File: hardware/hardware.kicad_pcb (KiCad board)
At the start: 2 copper layers, 76 x 60.5 mm, 159 parts, among them J1 USB_B_Micro, U1 CH32V003F4P6, U10 CH32V003F4P6, U11 CH32V003F4P6, U12 CH32V003F4P6, U13 CH32V003F4P6, U14 CH32V003F4P6, U15 CH32V003F4P6, U16 CH32V003F4P6, U17 CH32V003F4P6, U18 CH32V003F4P6, U19 CH32V003F4P6, U2 CH32V003F4P6, U20 CH32V003F4P6, U21 CH32V003F4P6, U22 CH32V003F4P6, U23 CH32V003F4P6, U24 CH32V003F4P6, U25 CH32V003F4P6, U26 CH32V003F4P6, U27 CH32V003F4P6, U3 AMS1117-3.3, U4 CH340C, U5 CH32V003F4P6, U6 CH32V003F4P6, U7 CH32V003F4P6, U8 CH32V003F4P6, U9 CH32V003F4P6

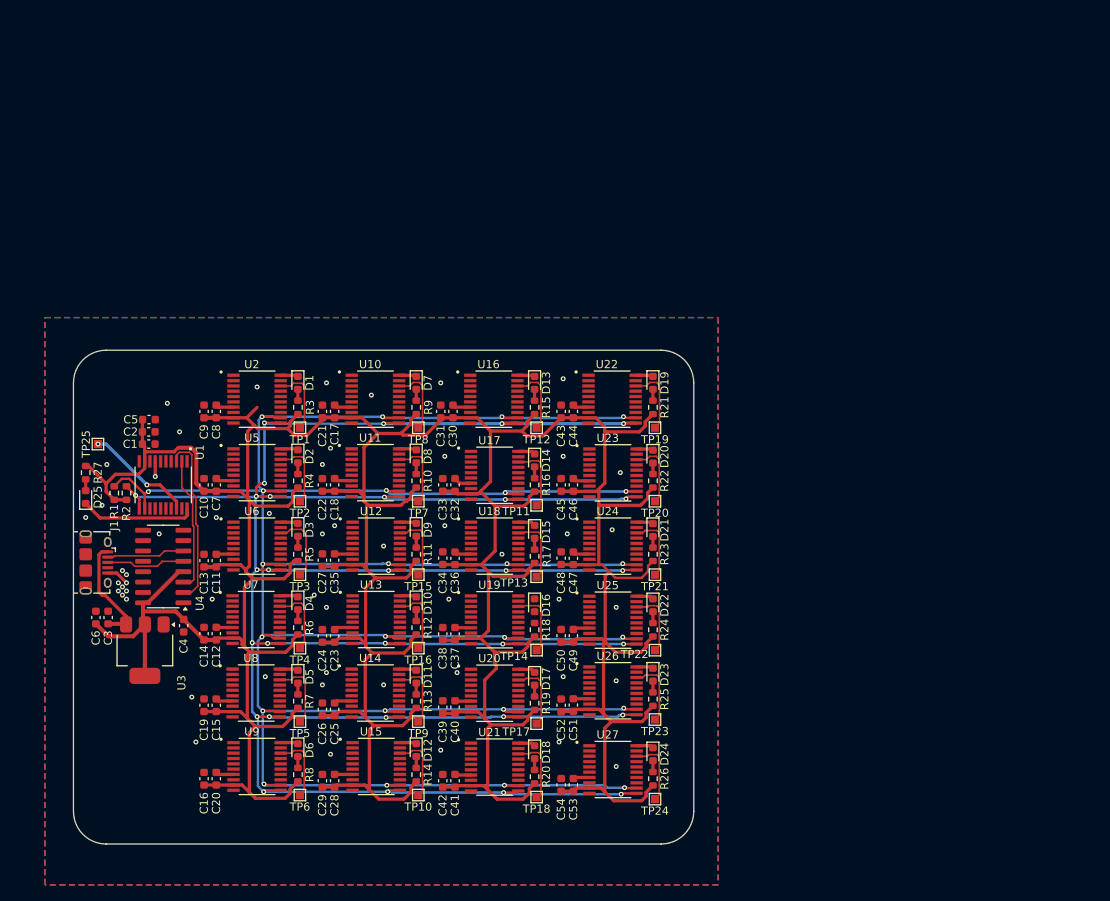
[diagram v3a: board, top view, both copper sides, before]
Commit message: add ethernet wiring
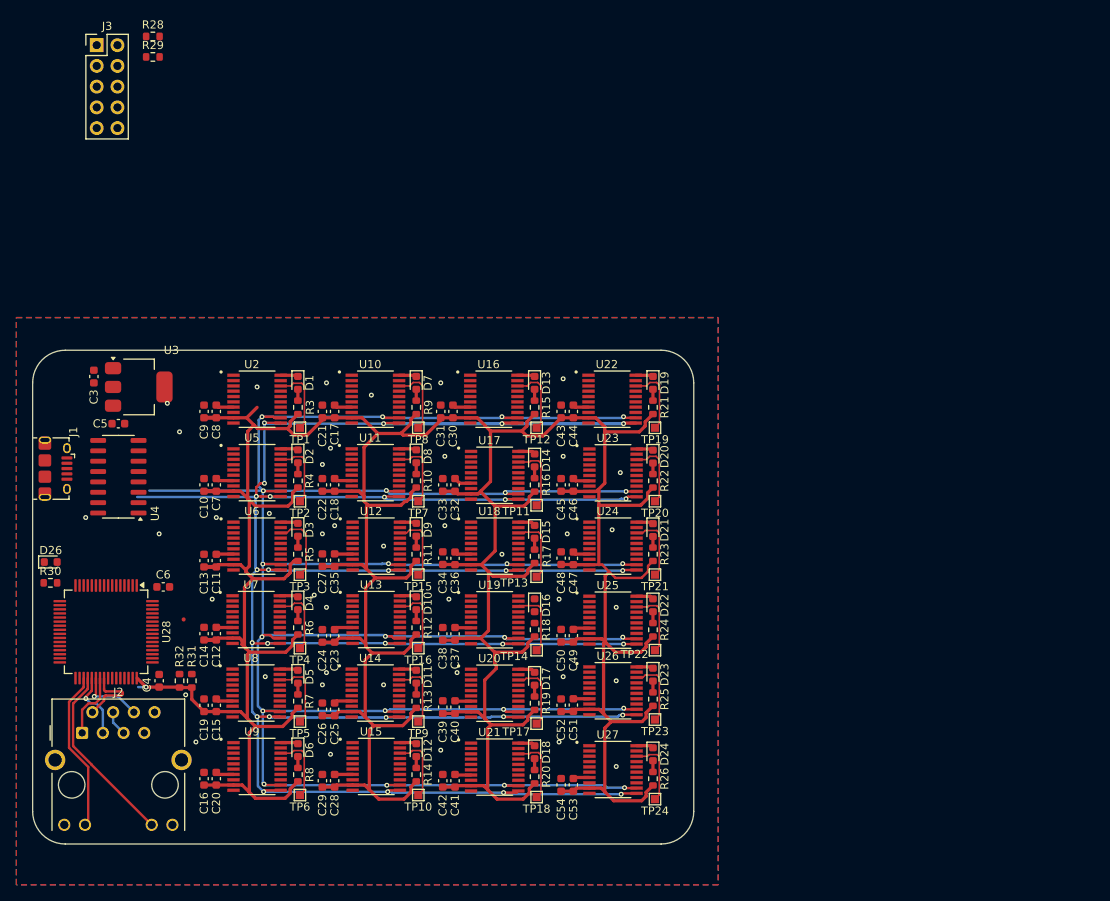
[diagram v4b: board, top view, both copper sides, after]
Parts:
- removed C1, C2: C_Small, Capacitor_SMD:C_0603_1608Metric
- removed D25: LED, LED_SMD:LED_0603_1608Metric
- removed R1, R2, R27: R_Small, Resistor_SMD:R_0603_1608Metric
- removed TP25: TestPoint, TestPoint:TestPoint_Pad_1.0x1.0mm
- removed U1: CH32V003F4P6, CH32V003F4P6:SOP65P640X121-20N
- added D26: LED, LED_SMD:LED_0603_1608Metric, F.Cu at (37.7, 69.0)
- added J2: RJ45_Hanrun_HR911105A_Horizontal, Connector_RJ:RJ45_Hanrun_HR911105A_Horizontal, F.Cu at (41.6, 89.9)
- added J3: Conn_02x05_Odd_Even, Connector_PinHeader_2.54mm:PinHeader_2x05_P2.54mm_Vertical, F.Cu at (43.4, 5.62)
- added R28: R_Small, Resistor_SMD:R_0603_1608Metric, F.Cu at (50.2, 4.55)
- added R29: R_Small, Resistor_SMD:R_0603_1608Metric, F.Cu at (50.2, 7.07)
- added R30: R_Small, Resistor_SMD:R_0603_1608Metric, F.Cu at (37.7, 71.5)
- added R31: R_Small, Resistor_SMD:R_0603_1608Metric, F.Cu at (55.0, 83.5)
- added R32: R_Small, Resistor_SMD:R_0603_1608Metric, F.Cu at (53.5, 83.5)
- added U28: CH32V307RCT6, Package_QFP:LQFP-64_10x10mm_P0.5mm, F.Cu at (44.5, 77.5)
- moved U3 32.3 mm to (48.5, 47.5), turned to 0 degrees
- moved C3 29.6 mm to (43.0, 46.2)
- moved J1 12.5 mm to (38.3, 57.5)
- moved U4 12.3 mm to (46.0, 58.5)
- moved C6 9.06 mm to (51.5, 72.0), turned to 0 degrees
- moved C4 7.39 mm to (51.0, 83.5), turned to 90 degrees
- moved C5 3.78 mm to (46.0, 52.0)
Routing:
- net +3V3: track 572.7 -> 524.9 mm, vias 0 -> 1
- net LED1: track 0.00 -> 22.7 mm
- net TX-PROG: track 21.4 -> 0.00 mm
- net LED2: track 0.00 -> 19.9 mm
- net RX-PROG: track 16.5 -> 0.00 mm
- net Net-(D25-K): track 14.1 -> 0.00 mm
- net +5V: track 13.6 -> 0.00 mm
- net Net-(U1-PD1/SWIO/T1CH3N/AETR2): track 13.4 -> 0.00 mm, vias 2 -> 0
- net D+: track 9.73 -> 0.00 mm
- net D-: track 9.59 -> 0.00 mm
- net TDN: track 0.00 -> 8.99 mm
- net RDP: track 0.00 -> 8.28 mm, vias 0 -> 1
- net TDP: track 0.00 -> 8.12 mm
- net RDN: track 0.00 -> 7.98 mm, vias 0 -> 1
- net SCL: track 378.0 -> 370.6 mm, vias 25 -> 24
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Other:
- board size 76 x 60.5 mm -> 81 x 60.5 mm

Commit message: wiring ch32v307 + ethernet
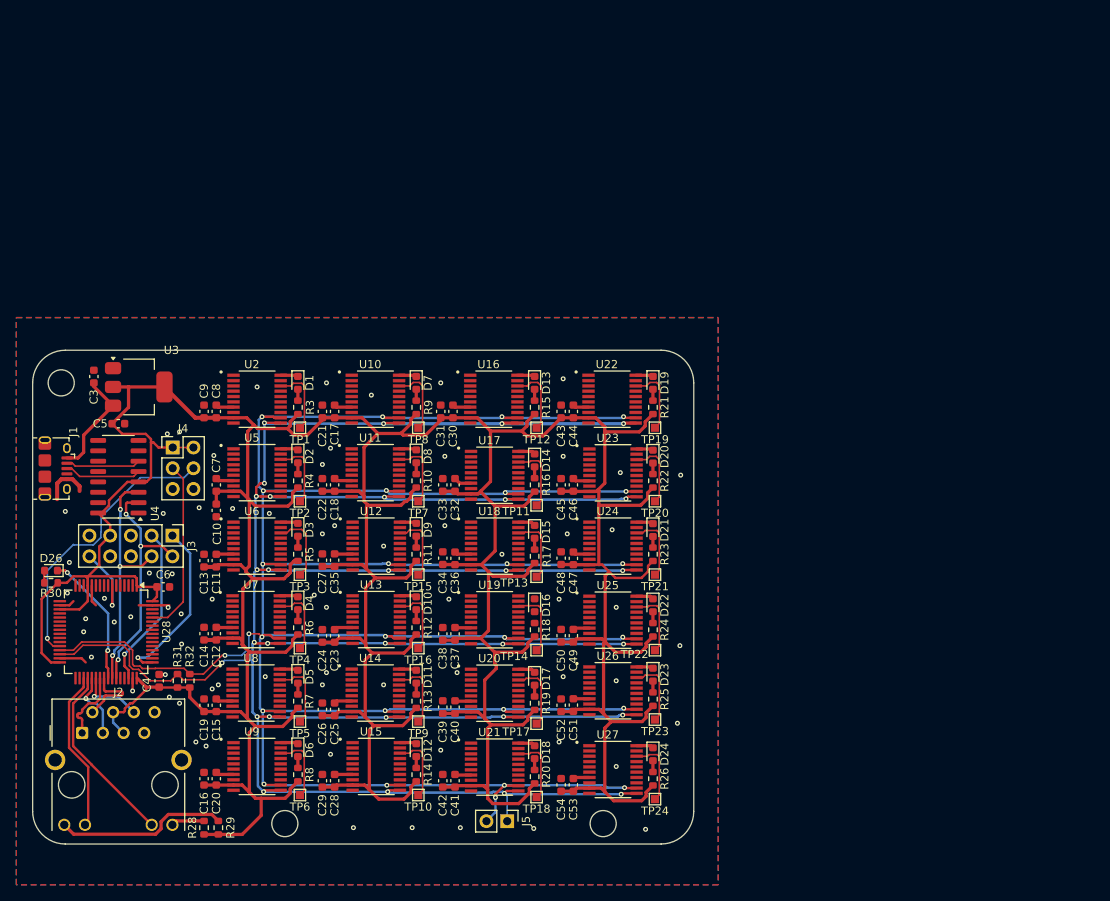
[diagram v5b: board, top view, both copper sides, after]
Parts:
- added J4: Conn_02x03_Odd_Even, Connector_PinHeader_2.54mm:PinHeader_2x03_P2.54mm_Vertical, F.Cu at (52.7, 54.9)
- added J5: Conn_01x02, Connector_PinHeader_2.54mm:PinHeader_1x02_P2.54mm_Vertical, F.Cu at (93.6, 100.7)
- moved R28 97.1 mm to (56.5, 101.5), turned to 90 degrees
- moved R29 94.8 mm to (58.2, 101.5), turned to 90 degrees
- moved J3 60.8 mm to (52.6, 65.7), turned to -90 degrees
- moved C10 3.47 mm to (58.0, 62.6), turned to -90 degrees
- moved R31 1.75 mm to (53.2, 83.5)
- moved R32 1.25 mm to (54.8, 83.5)
- moved D26 1.05 mm to (37.8, 70.0), turned to 180 degrees
- moved R30 0.08 mm to (37.8, 71.5)
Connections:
- J3 pad 2: TX -> TX-PROG
- J3 pad 4: RX -> RX-PROG
- U28 pad 52: LED2 -> unconnected-(U28-PC11-Pad52)
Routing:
- net +3V3: track 524.9 -> 625.5 mm, vias 1 -> 0
- net BOOT1: track 0.00 -> 35.0 mm, vias 0 -> 1
- net RX-PROG: track 0.00 -> 29.5 mm, vias 0 -> 3
- net TX-PROG: track 0.00 -> 29.3 mm, vias 0 -> 3
- net SCL: track 370.6 -> 392.9 mm, vias 24 -> 27
- net BOOT0: track 0.00 -> 21.5 mm
- net SWCLK: track 0.00 -> 21.2 mm, vias 0 -> 1
- net Net-(J2-Pad9): track 0.00 -> 21.2 mm
- net SWDIO: track 0.00 -> 20.0 mm, vias 0 -> 1
- net GND: track 50.7 -> 69.8 mm, vias 42 -> 72
- net SDA: track 370.9 -> 388.4 mm, vias 29 -> 30
- net Net-(D26-K): track 0.00 -> 16.5 mm, vias 0 -> 2
- net +5V: track 0.00 -> 13.3 mm
- net RST: track 0.00 -> 9.58 mm, vias 0 -> 1
- net D+: track 0.00 -> 9.42 mm
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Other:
- outline, holes or cut-outs redrawn

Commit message: add external crystal
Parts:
- added C1: 10pf, Capacitor_SMD:C_0603_1608Metric, F.Cu at (43.0, 68.5)
- added C2: 10pf, Capacitor_SMD:C_0603_1608Metric, F.Cu at (48.8, 68.5)
- added Y1: Crystal, Crystal:Crystal_SMD_3225-4Pin_3.2x2.5mm, F.Cu at (45.9, 68.6)
- moved J4 18.6 mm to (40.4, 68.9), turned to 180 degrees
- moved D26 12.8 mm to (37.6, 82.8)
- moved R30 12.8 mm to (37.6, 84.3)
- moved J3 2.59 mm to (55.1, 65.1), turned to 180 degrees
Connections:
- U28 pad 5: unconnected-(U28-OSC_IN/PD0-Pad5) -> XTAL2
- U28 pad 6: unconnected-(U28-OSC_OUT/PD1-Pad6) -> XTAL1
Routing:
- net BOOT1: track 35.0 -> 14.7 mm
- net RST: track 9.58 -> 26.5 mm
- net Net-(D26-K): track 16.5 -> 7.70 mm, vias 2 -> 0
- net XTAL1: track 0.00 -> 7.68 mm
- net XTAL2: track 0.00 -> 7.48 mm
- net BOOT0: track 21.5 -> 16.7 mm, vias 0 -> 1
- net SWDIO: track 20.0 -> 24.3 mm
- net +3V3: track 625.5 -> 628.6 mm
- net TX-PROG: track 29.3 -> 26.9 mm, vias 3 -> 1
- net Net-(D16-K): track 0.00 -> 2.15 mm
- net Net-(D16-A): track 0.00 -> 1.39 mm
- net RX-PROG: track 29.5 -> 28.7 mm, vias 3 -> 1
- net GND: vias 72 -> 69

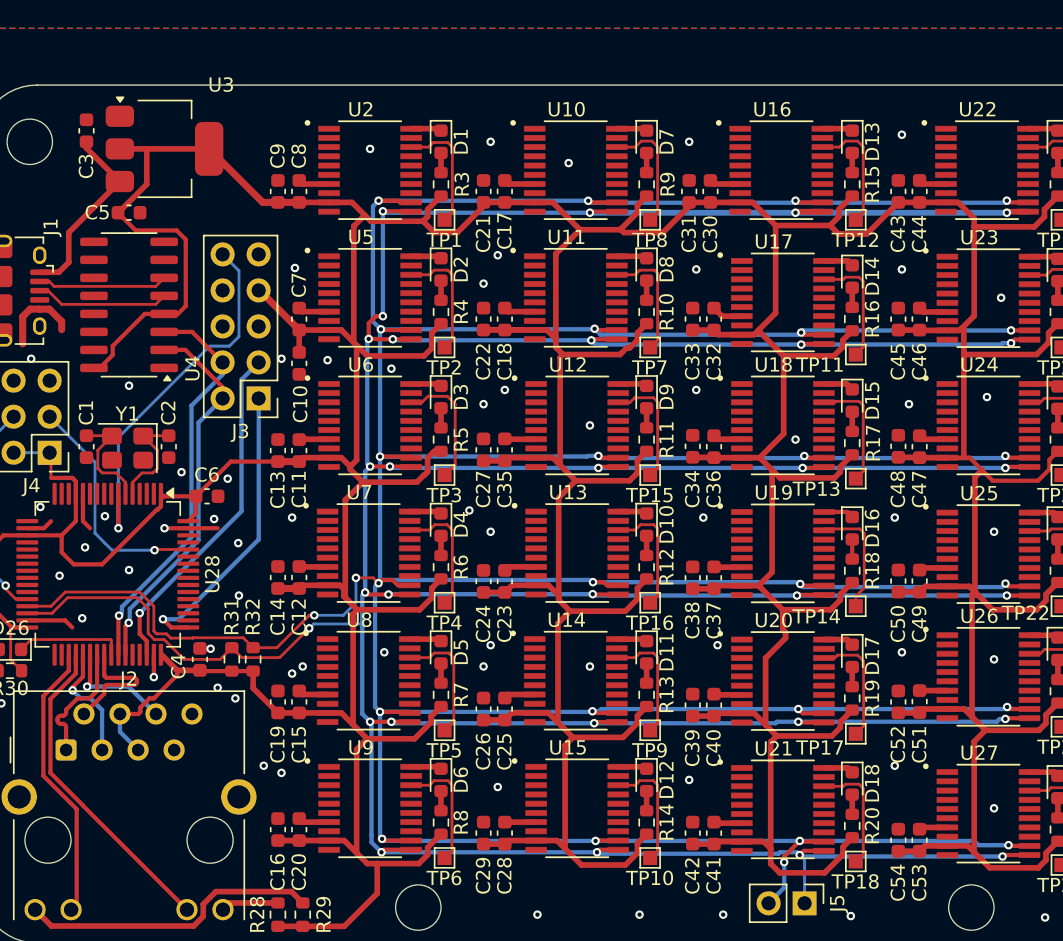
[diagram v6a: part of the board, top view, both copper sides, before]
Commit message: update crystal + slave reset pull up
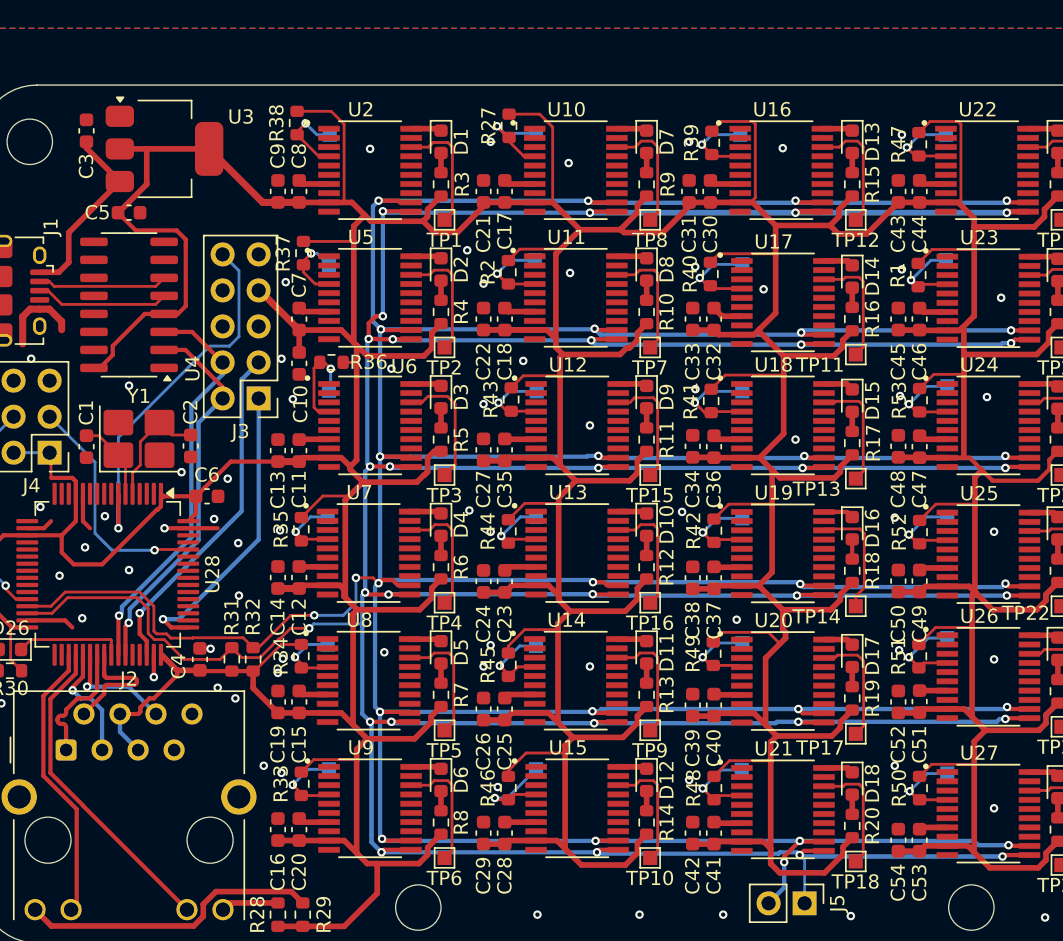
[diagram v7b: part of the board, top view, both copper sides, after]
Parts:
- added R1: R_Small, Resistor_SMD:R_0603_1608Metric, F.Cu at (101.7, 56.4)
- added R2: R_Small, Resistor_SMD:R_0603_1608Metric, F.Cu at (72.8, 56.2)
- added R27: R_Small, Resistor_SMD:R_0603_1608Metric, F.Cu at (72.8, 45.9)
- added R33: R_Small, Resistor_SMD:R_0603_1608Metric, F.Cu at (58.1, 92.3)
- added R34: R_Small, Resistor_SMD:R_0603_1608Metric, F.Cu at (58.1, 83.3)
- added R35: R_Small, Resistor_SMD:R_0603_1608Metric, F.Cu at (58.1, 74.3)
- added R36: R_Small, Resistor_SMD:R_0603_1608Metric, F.Cu at (60.3, 62.5)
- added R37: R_Small, Resistor_SMD:R_0603_1608Metric, F.Cu at (58.3, 54.9)
- added R38: R_Small, Resistor_SMD:R_0603_1608Metric, F.Cu at (57.9, 45.7)
- added R39: R_Small, Resistor_SMD:R_0603_1608Metric, F.Cu at (87.1, 47.1)
- added R40: R_Small, Resistor_SMD:R_0603_1608Metric, F.Cu at (87.0, 56.3)
- added R41: R_Small, Resistor_SMD:R_0603_1608Metric, F.Cu at (87.0, 65.3)
- added R42: R_Small, Resistor_SMD:R_0603_1608Metric, F.Cu at (87.2, 74.4)
- added R43: R_Small, Resistor_SMD:R_0603_1608Metric, F.Cu at (73.0, 65.2)
- added R44: R_Small, Resistor_SMD:R_0603_1608Metric, F.Cu at (72.8, 74.5)
- added R45: R_Small, Resistor_SMD:R_0603_1608Metric, F.Cu at (72.8, 83.9)
- added R46: R_Small, Resistor_SMD:R_0603_1608Metric, F.Cu at (72.8, 92.6)
- added R47: R_Small, Resistor_SMD:R_0603_1608Metric, F.Cu at (101.7, 47.2)
- added R48: R_Small, Resistor_SMD:R_0603_1608Metric, F.Cu at (87.2, 92.6)
- added R49: R_Small, Resistor_SMD:R_0603_1608Metric, F.Cu at (87.2, 83.1)
- added R50: R_Small, Resistor_SMD:R_0603_1608Metric, F.Cu at (101.8, 92.6)
- added R51: R_Small, Resistor_SMD:R_0603_1608Metric, F.Cu at (101.7, 83.3)
- added R52: R_Small, Resistor_SMD:R_0603_1608Metric, F.Cu at (101.8, 74.5)
- added R53: R_Small, Resistor_SMD:R_0603_1608Metric, F.Cu at (101.8, 65.2)
- added TP25: TestPoint, TestPoint:TestPoint_Pad_1.0x1.0mm, B.Cu at (103.6, 55.4)
- added TP26: TestPoint, TestPoint:TestPoint_Pad_1.0x1.0mm, B.Cu at (74.6, 55.4)
- added TP27: TestPoint, TestPoint:TestPoint_Pad_1.0x1.0mm, B.Cu at (74.7, 46.4)
- added TP28: TestPoint, TestPoint:TestPoint_Pad_1.0x1.0mm, B.Cu at (60.1, 91.2)
- added TP29: TestPoint, TestPoint:TestPoint_Pad_1.0x1.0mm, B.Cu at (60.0, 82.5)
- added TP30: TestPoint, TestPoint:TestPoint_Pad_1.0x1.0mm, B.Cu at (60.0, 73.5)
- added TP31: TestPoint, TestPoint:TestPoint_Pad_1.0x1.0mm, B.Cu at (60.1, 64.5)
- added TP32: TestPoint, TestPoint:TestPoint_Pad_1.0x1.0mm, B.Cu at (60.1, 55.7)
- added TP33: TestPoint, TestPoint:TestPoint_Pad_1.0x1.0mm, B.Cu at (60.1, 46.5)
- added TP34: TestPoint, TestPoint:TestPoint_Pad_1.0x1.0mm, B.Cu at (89.1, 46.5)
- added TP35: TestPoint, TestPoint:TestPoint_Pad_1.0x1.0mm, B.Cu at (89.2, 55.6)
- added TP36: TestPoint, TestPoint:TestPoint_Pad_1.0x1.0mm, B.Cu at (89.2, 64.6)
- added TP37: TestPoint, TestPoint:TestPoint_Pad_1.0x1.0mm, B.Cu at (89.2, 73.5)
- added TP38: TestPoint, TestPoint:TestPoint_Pad_1.0x1.0mm, B.Cu at (74.8, 64.6)
- added TP39: TestPoint, TestPoint:TestPoint_Pad_1.0x1.0mm, B.Cu at (74.7, 73.5)
- added TP40: TestPoint, TestPoint:TestPoint_Pad_1.0x1.0mm, B.Cu at (74.7, 82.5)
- added TP41: TestPoint, TestPoint:TestPoint_Pad_1.0x1.0mm, B.Cu at (74.7, 91.2)
- added TP42: TestPoint, TestPoint:TestPoint_Pad_1.0x1.0mm, B.Cu at (103.6, 46.5)
- added TP43: TestPoint, TestPoint:TestPoint_Pad_1.0x1.0mm, B.Cu at (89.2, 91.3)
- added TP44: TestPoint, TestPoint:TestPoint_Pad_1.0x1.0mm, B.Cu at (89.2, 82.3)
- added TP45: TestPoint, TestPoint:TestPoint_Pad_1.0x1.0mm, B.Cu at (103.7, 91.5)
- added TP46: TestPoint, TestPoint:TestPoint_Pad_1.0x1.0mm, B.Cu at (103.7, 82.0)
- added TP47: TestPoint, TestPoint:TestPoint_Pad_1.0x1.0mm, B.Cu at (103.7, 73.5)
- added TP48: TestPoint, TestPoint:TestPoint_Pad_1.0x1.0mm, B.Cu at (103.7, 64.2)
- Y1: value Crystal -> Crystal_GND24; footprint Crystal:Crystal_SMD_3225-4Pin_3.2x2.5mm -> Crystal:Crystal_SMD_3225-4Pin_3.2x2.5mm_HandSoldering
- moved C2 1.55 mm to (50.4, 68.5)
- moved Y1 1.03 mm to (46.7, 68.0), turned to 0 degrees
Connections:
- U10 pad 4: unconnected-(U10-PD7/~{RST}/T2CH4/OPP1-Pad4) -> Net-(U10-PD7/~{RST}/T2CH4/OPP1)
- U11 pad 4: unconnected-(U11-PD7/~{RST}/T2CH4/OPP1-Pad4) -> Net-(U11-PD7/~{RST}/T2CH4/OPP1)
- U12 pad 4: unconnected-(U12-PD7/~{RST}/T2CH4/OPP1-Pad4) -> Net-(U12-PD7/~{RST}/T2CH4/OPP1)
- U13 pad 4: unconnected-(U13-PD7/~{RST}/T2CH4/OPP1-Pad4) -> Net-(U13-PD7/~{RST}/T2CH4/OPP1)
- U14 pad 4: unconnected-(U14-PD7/~{RST}/T2CH4/OPP1-Pad4) -> Net-(U14-PD7/~{RST}/T2CH4/OPP1)
- U15 pad 4: unconnected-(U15-PD7/~{RST}/T2CH4/OPP1-Pad4) -> Net-(U15-PD7/~{RST}/T2CH4/OPP1)
- U16 pad 4: unconnected-(U16-PD7/~{RST}/T2CH4/OPP1-Pad4) -> Net-(U16-PD7/~{RST}/T2CH4/OPP1)
- U17 pad 4: unconnected-(U17-PD7/~{RST}/T2CH4/OPP1-Pad4) -> Net-(U17-PD7/~{RST}/T2CH4/OPP1)
- U18 pad 4: unconnected-(U18-PD7/~{RST}/T2CH4/OPP1-Pad4) -> Net-(U18-PD7/~{RST}/T2CH4/OPP1)
- U19 pad 4: unconnected-(U19-PD7/~{RST}/T2CH4/OPP1-Pad4) -> Net-(U19-PD7/~{RST}/T2CH4/OPP1)
- U2 pad 4: unconnected-(U2-PD7/~{RST}/T2CH4/OPP1-Pad4) -> Net-(U2-PD7/~{RST}/T2CH4/OPP1)
- U20 pad 4: unconnected-(U20-PD7/~{RST}/T2CH4/OPP1-Pad4) -> Net-(U20-PD7/~{RST}/T2CH4/OPP1)
- U21 pad 4: unconnected-(U21-PD7/~{RST}/T2CH4/OPP1-Pad4) -> Net-(U21-PD7/~{RST}/T2CH4/OPP1)
- U22 pad 4: unconnected-(U22-PD7/~{RST}/T2CH4/OPP1-Pad4) -> Net-(U22-PD7/~{RST}/T2CH4/OPP1)
- U23 pad 4: unconnected-(U23-PD7/~{RST}/T2CH4/OPP1-Pad4) -> Net-(U23-PD7/~{RST}/T2CH4/OPP1)
- U24 pad 4: unconnected-(U24-PD7/~{RST}/T2CH4/OPP1-Pad4) -> Net-(U24-PD7/~{RST}/T2CH4/OPP1)
- U25 pad 4: unconnected-(U25-PD7/~{RST}/T2CH4/OPP1-Pad4) -> Net-(U25-PD7/~{RST}/T2CH4/OPP1)
- U26 pad 4: unconnected-(U26-PD7/~{RST}/T2CH4/OPP1-Pad4) -> Net-(U26-PD7/~{RST}/T2CH4/OPP1)
- U27 pad 4: unconnected-(U27-PD7/~{RST}/T2CH4/OPP1-Pad4) -> Net-(U27-PD7/~{RST}/T2CH4/OPP1)
- U5 pad 4: unconnected-(U5-PD7/~{RST}/T2CH4/OPP1-Pad4) -> Net-(U5-PD7/~{RST}/T2CH4/OPP1)
- U6 pad 4: unconnected-(U6-PD7/~{RST}/T2CH4/OPP1-Pad4) -> Net-(U6-PD7/~{RST}/T2CH4/OPP1)
- U7 pad 4: unconnected-(U7-PD7/~{RST}/T2CH4/OPP1-Pad4) -> Net-(U7-PD7/~{RST}/T2CH4/OPP1)
- U8 pad 4: unconnected-(U8-PD7/~{RST}/T2CH4/OPP1-Pad4) -> Net-(U8-PD7/~{RST}/T2CH4/OPP1)
- U9 pad 4: unconnected-(U9-PD7/~{RST}/T2CH4/OPP1-Pad4) -> Net-(U9-PD7/~{RST}/T2CH4/OPP1)
- Y1 pad 1: XTAL2 -> XTAL1
- Y1 pad 2: XTAL1 -> GND
- Y1 pad 3: (no net) -> XTAL2
- Y1 pad 4: (no net) -> GND
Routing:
- net +3V3: track 628.6 -> 749.1 mm
- net Net-(U18-PD7/~{RST}/T2CH4/OPP1): track 0.00 -> 7.31 mm, vias 0 -> 1
- net Net-(U6-PD7/~{RST}/T2CH4/OPP1): track 0.00 -> 7.08 mm, vias 0 -> 1
- net Net-(U15-PD7/~{RST}/T2CH4/OPP1): track 0.00 -> 6.87 mm, vias 0 -> 1
- net Net-(U17-PD7/~{RST}/T2CH4/OPP1): track 0.00 -> 6.66 mm, vias 0 -> 1
- net Net-(U10-PD7/~{RST}/T2CH4/OPP1): track 0.00 -> 6.66 mm, vias 0 -> 1
- net Net-(U21-PD7/~{RST}/T2CH4/OPP1): track 0.00 -> 6.50 mm, vias 0 -> 1
- net Net-(U26-PD7/~{RST}/T2CH4/OPP1): track 0.00 -> 6.45 mm, vias 0 -> 1
- net Net-(U19-PD7/~{RST}/T2CH4/OPP1): track 0.00 -> 6.35 mm, vias 0 -> 1
- net Net-(U25-PD7/~{RST}/T2CH4/OPP1): track 0.00 -> 6.30 mm, vias 0 -> 1
- net Net-(U20-PD7/~{RST}/T2CH4/OPP1): track 0.00 -> 6.26 mm, vias 0 -> 1
- net Net-(U14-PD7/~{RST}/T2CH4/OPP1): track 0.00 -> 6.26 mm, vias 0 -> 1
- net Net-(U24-PD7/~{RST}/T2CH4/OPP1): track 0.00 -> 6.17 mm, vias 0 -> 1
- net Net-(U22-PD7/~{RST}/T2CH4/OPP1): track 0.00 -> 6.14 mm, vias 0 -> 1
- net Net-(U27-PD7/~{RST}/T2CH4/OPP1): track 0.00 -> 6.08 mm, vias 0 -> 1
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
